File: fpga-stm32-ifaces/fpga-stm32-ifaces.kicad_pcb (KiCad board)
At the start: 6 copper layers, 90 x 94.5 mm, 273 parts, among them J1 0826-1G1T-23-F, J10 CORTEX_DEBUG_ETM, J11 XILINX_JTAG, J12 CONN_01X03, J2 PMOD_HOST, J3 PMOD_HOST, J4 XILINX_JTAG, J5 CONN_01X03, J6 CONN_01X03, J7 CONN_PCIE_PWR_8PIN, J8 XILINX_JTAG, J9 CONN_IBC_MGMT_DEVICE, M1 LOGO, M2 LOGO, M3 LOGO, M5 SCREWHOLE, M6 SCREWHOLE, M7 SCREWHOLE, M8 SCREWHOLE, U1 STM32H735-UFBGA176-25, U10 ECS-1612MV-250-CN, U11 STM32L431-QFN48, U12 MUN12AD03-SE, U13 MUN12AD03-SE, U14 MUN12AD03-SE, U15 MUN12AD03-SE, U16 W25Q128JV, U2 XC7S25-1FTGB196, U3 S25FL128SAGBHIA10, U4 KSZ9031RN, U5 RCLAMP0514M, U6 RCLAMP0514M, U7 ECS-1612MV-250-CN, U8 AT24MAC402, U9 ECS-1612MV-250-CN

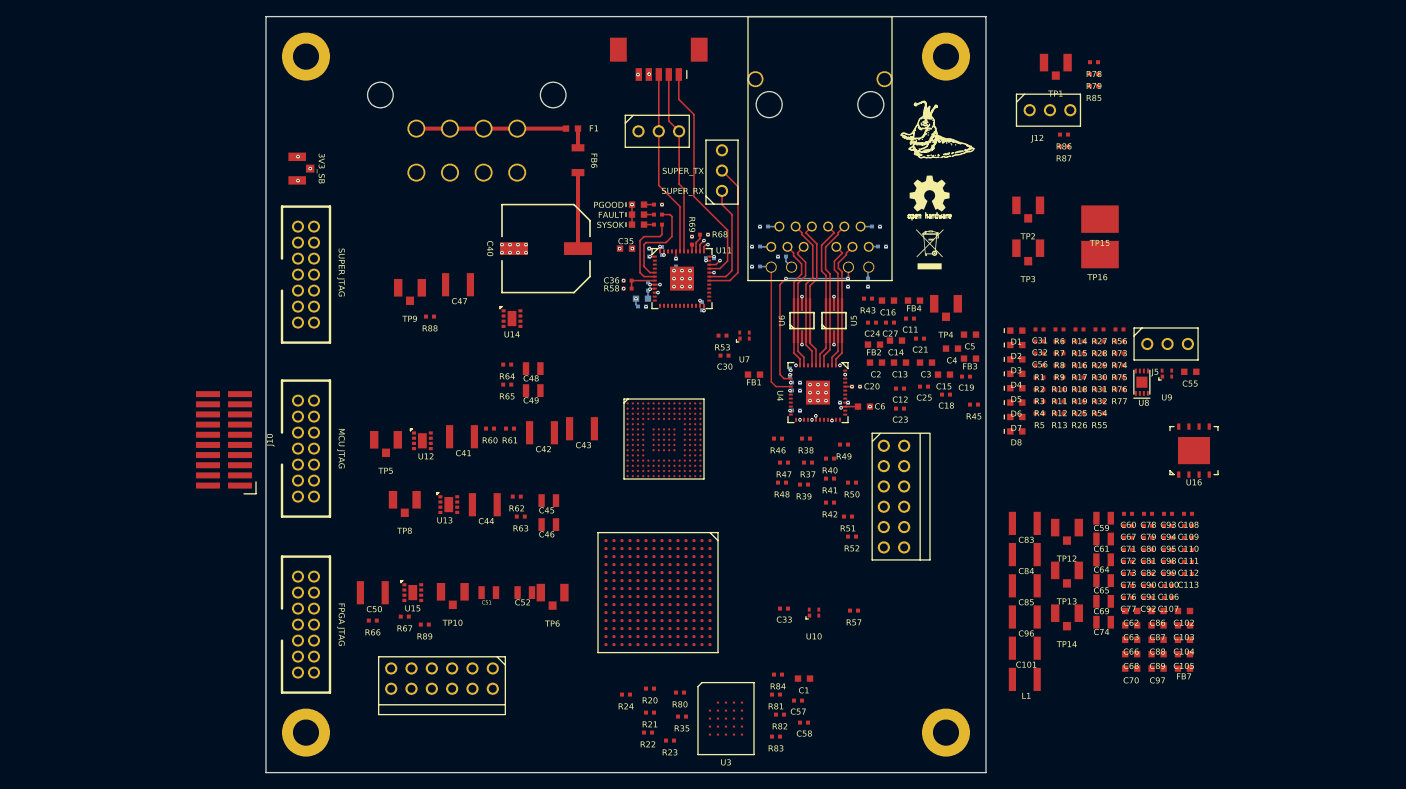
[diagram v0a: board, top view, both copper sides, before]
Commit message: Initial routing of FPGA power
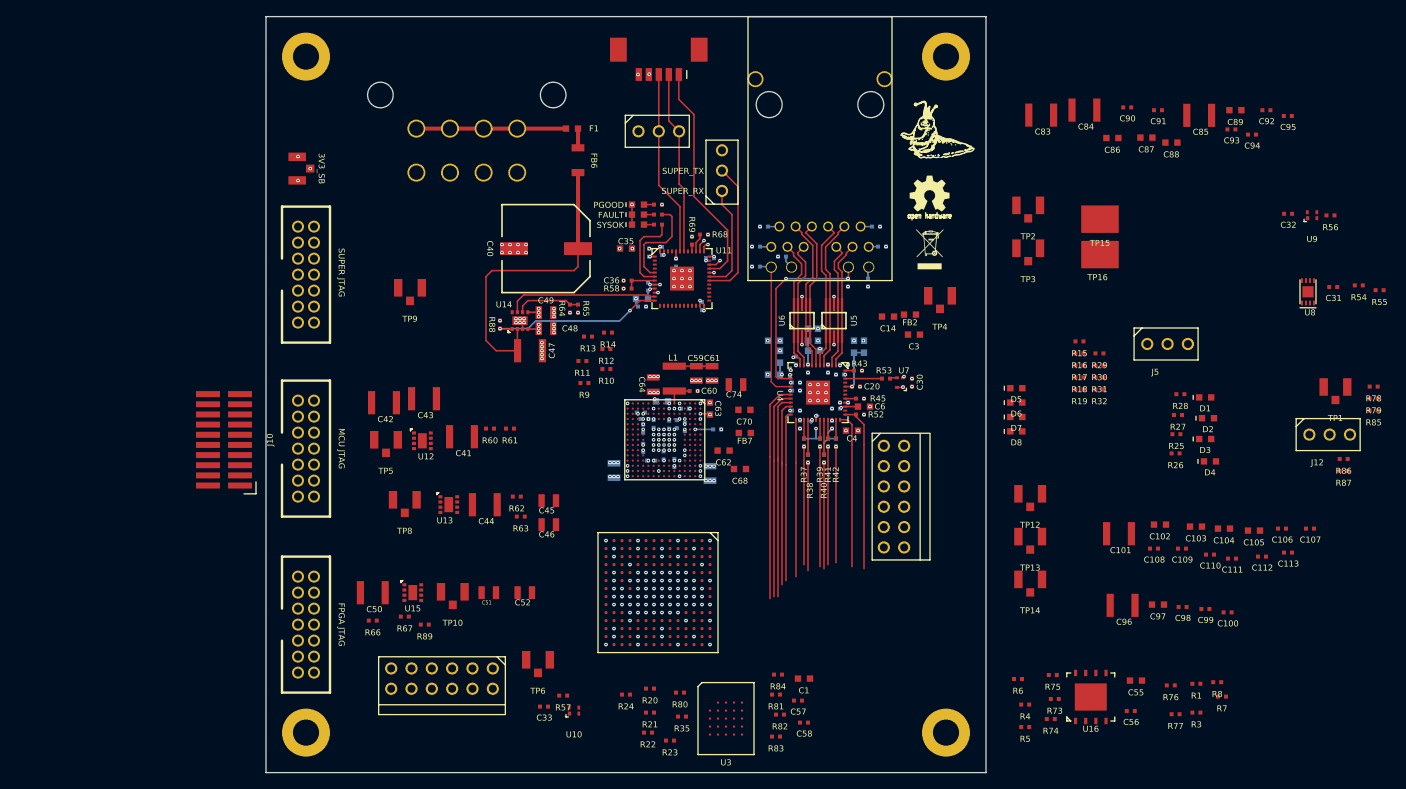
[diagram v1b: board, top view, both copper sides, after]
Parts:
- C11, C12, C13, C15, C16, C18, C19, C2, C21, C23, C24, C25, C27, C5, C65, C66, C67, C69, C71, C72, C73, C75, C76, C77, C78, C79, C80, C81, C82, FB1, FB3, FB4, R2, R46, R47, R48, R49, R50, R51: moved to B.Cu
- moved C89 68.7 mm to (149.2, 52.7)
- moved C66 65.8 mm to (77.5, 89.1), turned to 180 degrees
- moved C80 65.3 mm to (74.8, 90.5)
- moved C81 64.4 mm to (75.2, 94.9), turned to -90 degrees
- moved C77 64.2 mm to (75.2, 92.5), turned to -90 degrees
- moved C79 63.1 mm to (76.5, 91.9), turned to -90 degrees
- moved C73 63.0 mm to (75.3, 91.3)
- moved C65 62.7 mm to (71.5, 97.8), turned to -90 degrees
- moved C92 62.7 mm to (153.1, 52.7)
- moved C85 62.7 mm to (144.7, 53.3)
- moved FB7 62.3 mm to (87.8, 93.0)
- moved C88 62.2 mm to (141.2, 56.8)
- moved C87 61.0 mm to (138.1, 56.1)
- moved C72 60.6 mm to (76.2, 96.5), turned to 180 degrees
- moved C82 60.5 mm to (79.0, 96.8), turned to -90 degrees
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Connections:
- U11 pad 11: /FPGA_INIT -> /Power supply/1V2_PGOOD
- U11 pad 12: /MCU_RST_N -> /Power supply/1V2_EN
- U11 pad 26: /Power supply/1V2_PGOOD -> /MCU_RST_N
- U11 pad 32: /Power supply/1V2_EN -> /FPGA_INIT
- U2 pad B6: /MCU/RMII_TX_EN -> /MCU/FPGA_QSPI_DQ6
- U2 pad D1: /MCU/FMC_AD12 -> /MCU/FPGA_QSPI_DQ7
- U2 pad N1: /MCU/FPGA_QSPI_DQ7 -> /MCU/FMC_AD12
- U2 pad P2: /MCU/FPGA_QSPI_DQ6 -> /MCU/RMII_TX_EN
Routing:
- net /GND: track 357.0 -> 647.0 mm, vias 55 -> 210
- net /3V3: track 44.0 -> 189.1 mm, vias 5 -> 40
- net /Ethernet/1V2: track 0.00 -> 54.3 mm, vias 0 -> 11
- net /12V0: track 9.50 -> 39.1 mm
- net /Power supply/1V0: track 0.00 -> 28.6 mm, vias 0 -> 13
- net /Power support/VSMPS: track 0.00 -> 28.0 mm, vias 0 -> 5
- net /Ethernet/RGMII_TXD0: track 0.00 -> 27.4 mm
- net /Ethernet/RGMII_TXD1: track 0.00 -> 26.3 mm
- net /Ethernet/RGMII_TXD2: track 0.00 -> 25.8 mm
- net /Power supply/1V8: track 0.00 -> 23.4 mm, vias 0 -> 6
- net /Ethernet/RGMII_TXD3: track 0.00 -> 23.3 mm
- net /Power support/VCORE: track 0.00 -> 22.4 mm, vias 0 -> 9
- net /Power supply/1V2_EN: track 0.60 -> 22.3 mm, vias 1 -> 2
- net /Ethernet/RGMII_TX_CLK: track 0.00 -> 21.2 mm
- net /Ethernet/ETH_MDIO: track 0.00 -> 21.0 mm
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
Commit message: Routed most FPGA decoupling caps plus most of RGMII
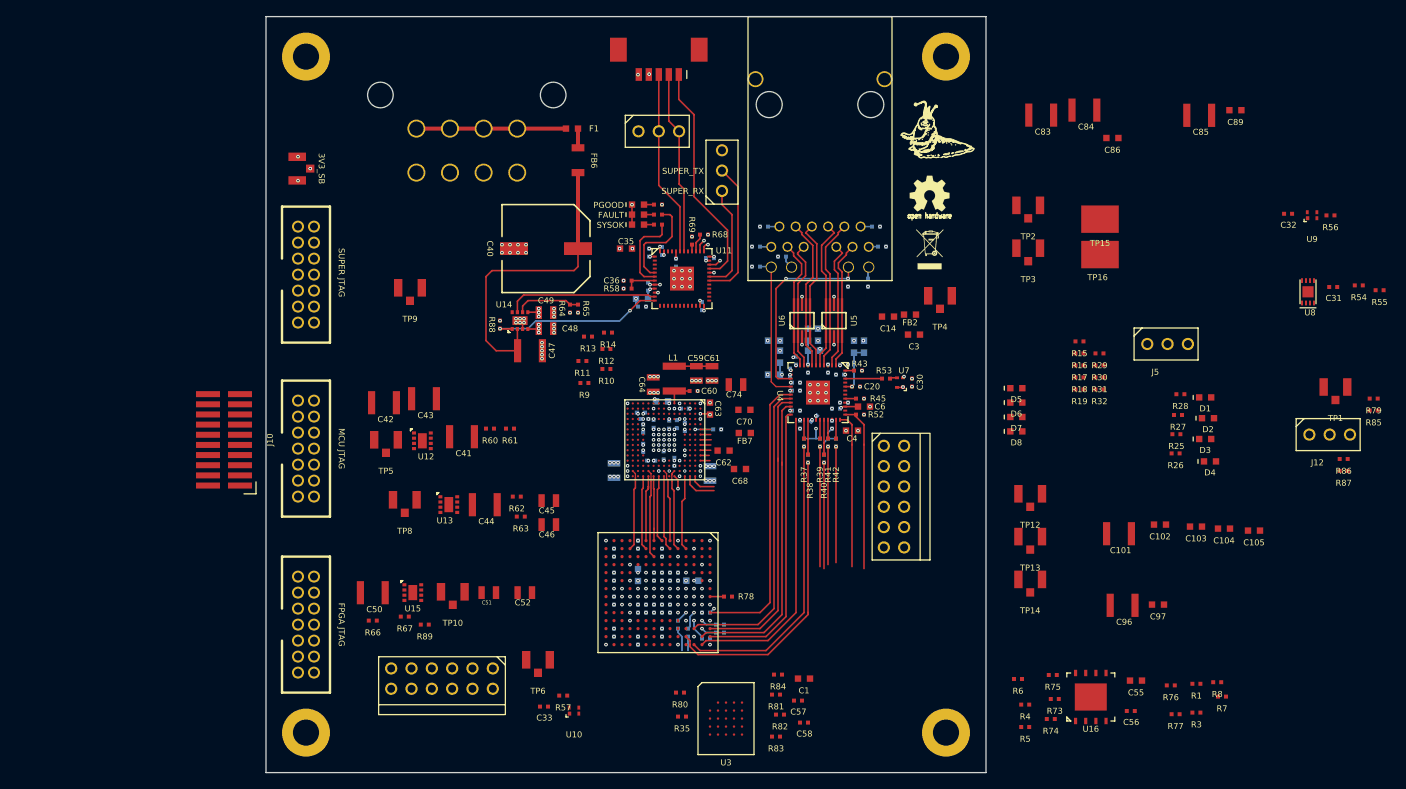
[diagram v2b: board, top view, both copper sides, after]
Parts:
- added R90: 1K, azonenberg_pcb:EIA_0402_RES_NOSILK, B.Cu at (83.0, 115.5)
- C100, C106, C107, C108, C109, C110, C111, C112, C113, C87, C88, C90, C91, C92, C93, C94, C95, C98, C99, R20, R21, R22, R23, R24: moved to B.Cu
- moved C92 97.9 mm to (77.5, 115.0), turned to -90 degrees
- moved C95 97.1 mm to (77.5, 111.0), turned to -90 degrees
- moved C94 93.0 mm to (76.5, 111.0), turned to 90 degrees
- moved C93 89.7 mm to (78.5, 111.0), turned to 90 degrees
- moved C91 89.3 mm to (75.5, 115.0), turned to -90 degrees
- moved C88 85.8 mm to (74.5, 110.8), turned to 90 degrees
- moved R78 84.9 mm to (85.8, 113.5)
- moved C106 83.7 mm to (71.5, 111.0), turned to 90 degrees
- moved C90 81.2 mm to (79.5, 111.0), turned to -90 degrees
- moved C107 81.1 mm to (77.5, 108.0), turned to -90 degrees
- moved C87 79.3 mm to (81.3, 111.5)
- moved C113 78.9 mm to (77.5, 118.0), turned to 90 degrees
- moved C112 78.7 mm to (74.5, 119.0), turned to -90 degrees
- moved C111 77.8 mm to (71.5, 118.0), turned to 90 degrees
- moved C110 74.7 mm to (71.5, 114.0), turned to -90 degrees
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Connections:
- U1 pad B8: /MCU/FMC_NE1 -> unconnected-(U1D-PD7-PadB8)
- U1 pad D15: unconnected-(U1C-PC7-PadD15) -> /MCU/FMC_NE1
- U1 pad K15: unconnected-(U1B-PB14-PadK15) -> /MCU/FMC_AD10
- U1 pad P13: /MCU/FMC_AD10 -> unconnected-(U1E-PE13-PadP13)
- U2 pad A10: /Ethernet/RGMII_TXD2 -> /Ethernet/RGMII_TXD0
- U2 pad A12: /Ethernet/RGMII_TXD1 -> /Ethernet/RGMII_TXD2
- U2 pad A13: /Ethernet/RGMII_TXD0 -> /Ethernet/RGMII_TX_CLK
- U2 pad A3: /MCU/FMC_NE1 -> /MCU/FMC_AD11
- U2 pad A5: /MCU/FMC_NE3 -> /MCU/RMII_RXD0
- U2 pad B10: unconnected-(U2C-IO_L3P_T0_DQS_PUDC_B_14-PadB10) -> Net-(U2C-IO_L3P_T0_DQS_PUDC_B_14)
- U2 pad B14: /Ethernet/RGMII_TX_CLK -> /Ethernet/RGMII_TX_EN
- U2 pad B2: /MCU/FMC_AD0 -> /MCU/FMC_AD9
- U2 pad C1: /MCU/FMC_AD13 -> /MCU/FPGA_QSPI_DQ0
- U2 pad C12: /Ethernet/ETH_RXD0 -> /Ethernet/RGMII_TXD1
- U2 pad C14: /Ethernet/ETH_RXD2 -> /Ethernet/ETH_RXD3
- U2 pad D13: /Ethernet/ETH_RXD3 -> /Ethernet/ETH_RXD2
- U2 pad D14: /Ethernet/RGMII_TX_EN -> /Ethernet/ETH_RXD0
- U2 pad D2: /MCU/FMC_AD11 -> /MCU/FMC_NE1
- U2 pad E2: /MCU/FMC_AD10 -> /MCU/FMC_NE3
- U2 pad F1: /MCU/FMC_AD9 -> /MCU/FMC_AD0
- U2 pad F2: /MCU/FMC_AD7 -> /MCU/FMC_A18
- U2 pad G1: /MCU/FMC_AD8 -> /MCU/FMC_A17
- U2 pad H1: /MCU/RMII_TXD0 -> /MCU/FMC_AD10
- U2 pad H3: /MCU/FPGA_QSPI_DQ0 -> /MCU/FMC_AD13
- U2 pad J1: /MCU/RMII_RXD0 -> /MCU/RMII_TXD1
- U2 pad J2: /MCU/RMII_TXD1 -> /MCU/RMII_TXD0
- U2 pad L2: /MCU/FPGA_LED_3 -> /MCU/FMC_AD12
- U2 pad L5: /MCU/FMC_A18 -> /MCU/FMC_AD7
- U2 pad N1: /MCU/FMC_AD12 -> /MCU/FPGA_LED_3
- U2 pad N4: /MCU/FMC_A17 -> /MCU/FMC_AD8
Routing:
- net /Ethernet/ETH_RXD2: track 13.5 -> 37.7 mm
- net /Ethernet/ETH_RXD3: track 14.8 -> 36.8 mm
- net /Ethernet/RGMII_TX_EN: track 19.6 -> 37.5 mm
- net /Ethernet/RGMII_TX_CLK: track 21.2 -> 36.2 mm
- net /Ethernet/RGMII_TXD3: track 23.3 -> 38.2 mm
- net /Ethernet/RGMII_TXD1: track 26.3 -> 38.8 mm
- net /Ethernet/RGMII_TXD2: track 25.8 -> 37.0 mm
- net /MCU/FMC_AD13: track 0.00 -> 11.1 mm
- net /MCU/FMC_NE3: track 0.00 -> 10.2 mm
- net /MCU/FMC_AD12: track 0.00 -> 10.1 mm
- net /MCU/FMC_NE1: track 0.00 -> 9.40 mm
- net /MCU/FMC_A18: track 0.00 -> 9.36 mm
- net /MCU/RMII_TXD0: track 0.00 -> 9.32 mm
- net /MCU/FMC_AD0: track 0.00 -> 9.01 mm
- net /Ethernet/RGMII_TXD0: track 27.4 -> 35.9 mm
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
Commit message: Continued layout, 283 now unrouted
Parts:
- C14, C3, C32, C70, FB2, FB7, R14, R15, R16, R18, R3, R56, R8, U9: moved to B.Cu
- moved R86 104.8 mm to (58.5, 85.7)
- moved R87 101.0 mm to (62.0, 104.8)
- moved R56 86.1 mm to (77.0, 84.4), turned to 90 degrees
- moved R7 83.1 mm to (70.9, 93.9)
- moved U9 83.1 mm to (77.4, 82.5), turned to -90 degrees
- moved R3 80.5 mm to (71.6, 93.5)
- moved R8 79.2 mm to (71.6, 99.8)
- moved C32 78.9 mm to (78.7, 82.4), turned to -90 degrees
- moved R1 65.9 mm to (86.6, 92.6), turned to 180 degrees
- moved R5 64.6 mm to (70.8, 91.6)
- moved R4 63.9 mm to (70.8, 90.0)
- moved R6 59.6 mm to (70.9, 93.1)
- moved R15 59.4 mm to (71.6, 94.2)
- moved R16 59.3 mm to (71.6, 95.0)
- moved TP9 58.7 mm to (104.5, 80.2), turned to -90 degrees
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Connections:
- U1 pad A8: /MCU/MCU_PMOD_DQ5 -> /MCU/MCU_PMOD_DQ7
- U1 pad D7: /MCU/MCU_PMOD_DQ4 -> /MCU/MCU_PMOD_DQ2
- U1 pad D9: /MCU/FMC_NWAIT -> unconnected-(U1D-PD6-PadD9)
- U1 pad E14: unconnected-(U1C-PC6-PadE14) -> /MCU/FMC_NWAIT
- U1 pad G13: /MCU/MCU_PMOD_DQ2 -> /MCU/MCU_PMOD_DQ4
- U1 pad G14: /MCU/MCU_PMOD_DQ7 -> /MCU/MCU_PMOD_DQ5
- U11 pad 13: /Power supply/1V0_EN -> /MCU_RST_N
- U11 pad 26: /MCU_RST_N -> /Power supply/1V0_EN
- U2 pad A3: /MCU/FMC_AD11 -> /MCU/FPGA_QSPI_DQS
- U2 pad C4: /MCU/FMC_AD3 -> /MCU/FPGA_QSPI_DQ7
- U2 pad D1: /MCU/FPGA_QSPI_DQ7 -> /MCU/FMC_AD3
- U2 pad E4: /MCU/FMC_AD4 -> /MCU/FPGA_LED_3
- U2 pad F3: /MCU/FMC_AD6 -> /MCU/FPGA_QSPI_DQ5
- U2 pad L1: /MCU/FPGA_QSPI_DQS -> /MCU/FMC_AD11
- U2 pad M1: /MCU/FPGA_QSPI_CS_N -> /MCU/FMC_AD8
- U2 pad M2: /MCU/FPGA_QSPI_DQ5 -> /MCU/FMC_AD6
- U2 pad N1: /MCU/FPGA_LED_3 -> /MCU/RMII_TX_EN
- U2 pad N4: /MCU/FMC_AD8 -> /MCU/FPGA_QSPI_CS_N
- U2 pad P2: /MCU/RMII_TX_EN -> /MCU/FMC_AD4
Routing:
- net /GND: track 647.0 -> 713.9 mm, vias 210 -> 234
- net /3V3: track 191.2 -> 252.3 mm, vias 41 -> 53
- net /MCU/MCU_UART_RX: track 4.36 -> 39.9 mm, vias 0 -> 1
- net /MCU/MCU_UART_TX: track 3.30 -> 37.6 mm, vias 0 -> 1
- net /MCU/MCU_PMOD_DQ3: track 0.00 -> 32.3 mm, vias 0 -> 3
- net /MCU/MCU_PMOD_DQ4: track 0.00 -> 32.2 mm, vias 0 -> 1
- net /MCU/MCU_PMOD_DQ7: track 0.00 -> 30.0 mm
- net /MCU/MCU_PMOD_DQ5: track 1.35 -> 31.2 mm, vias 0 -> 1
- net /MCU/MCU_PMOD_DQ0: track 0.00 -> 29.2 mm, vias 0 -> 1
- net /MCU/FMC_CLK: track 1.30 -> 30.1 mm, vias 0 -> 2
- net /MCU/MCU_PMOD_DQ1: track 0.00 -> 25.9 mm, vias 0 -> 2
- net /MCU/SUPER_SPI_SCK: track 0.00 -> 24.0 mm, vias 0 -> 3
- net /MCU/MCU_JTAG_TDO: track 0.00 -> 19.8 mm, vias 0 -> 2
- net /MCU/MCU_JTAG_TDI: track 1.10 -> 20.2 mm, vias 0 -> 2
- net /MCU/MCU_JTAG_TCK: track 1.20 -> 19.6 mm, vias 0 -> 2
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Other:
- board text added: "1V2"
- board text added: "GND"
- board text added: "MCU TRACE"
- board text added: "MCU_RX"
- board text added: "MCU_TX"
